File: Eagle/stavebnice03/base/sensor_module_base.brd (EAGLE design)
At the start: 19 parts

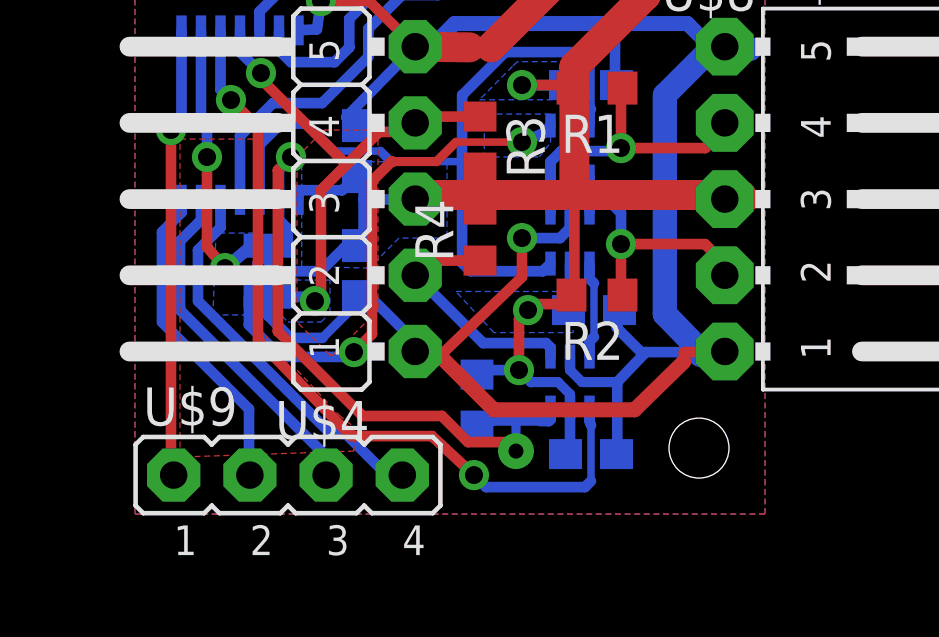
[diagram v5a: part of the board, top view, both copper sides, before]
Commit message: fix of bugs on rgb and lipol board + a few minor changes
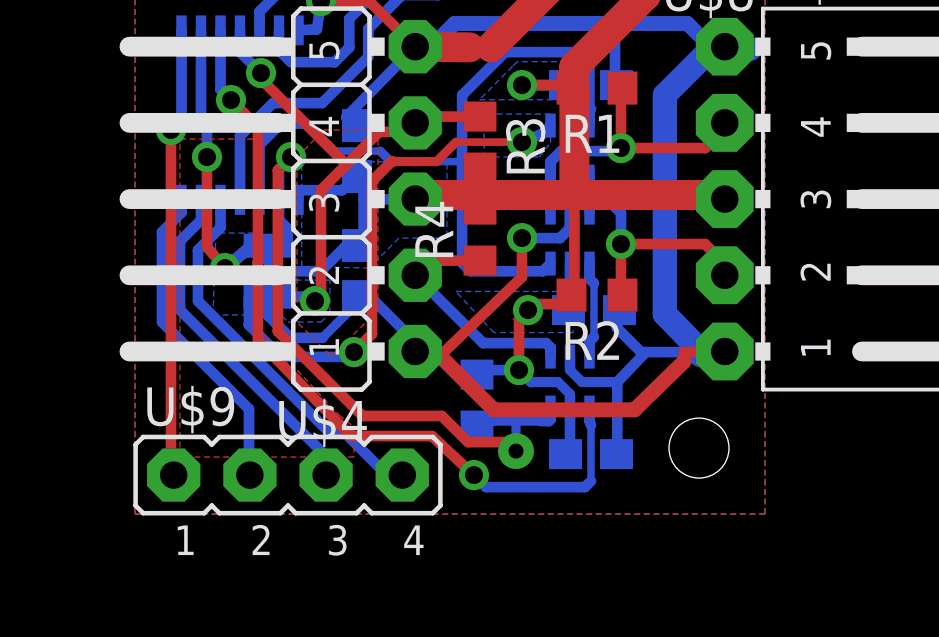
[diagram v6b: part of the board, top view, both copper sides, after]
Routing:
- net VCC: track 55.0 -> 53.9 mm
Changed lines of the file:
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@@
 <layer number="17" name="Pads" color="2" fill="1" visible="yes" active="yes"/>
 <layer number="18" name="Vias" color="2" fill="1" visible="yes" active="yes"/>
-<layer number="19" name="Unrouted" color="6" fill="1" visible="yes" active="yes"/>
+<layer number="19" name="Unrouted" color="6" fill="1" visible="no" active="yes"/>
 <layer number="20" name="Dimension" color="15" fill="1" visible="yes" active="yes"/>
 <layer number="21" name="tPlace" color="7" fill="1" visible="no" active="yes"/>
@@
 <text x="4.92125" y="-6.0325" size="2.54" layer="1" align="center">II=I+I</text>
 <text x="10.5" y="27" size="1.778" layer="20" align="center">sensor base</text>
-<wire x1="-10" y1="-10" x2="31" y2="-10" width="0.01" layer="49"/>
-<wire x1="31" y1="-10" x2="31" y2="31" width="0.01" layer="49"/>
-<wire x1="31" y1="31" x2="-10" y2="31" width="0.01" layer="49"/>
-<wire x1="-10" y1="31" x2="-10" y2="-10" width="0.01" layer="49"/>
+<wire x1="-10" y1="-10" x2="-2.5" y2="-10" width="0.01" layer="49"/>
+<wire x1="-2.5" y1="-10" x2="23.5" y2="-10" width="0.01" layer="49"/>
+<wire x1="23.5" y1="-10" x2="31" y2="-10" width="0.01" layer="49"/>
+<wire x1="31" y1="31" x2="23.5" y2="31" width="0.01" layer="49"/>
+<wire x1="23.5" y1="31" x2="-2.5" y2="31" width="0.01" layer="49"/>
+<wire x1="-2.5" y1="31" x2="-10" y2="31" width="0.01" layer="49"/>
 <circle x="2.2" y="18.8" radius="0.6" width="0.9" layer="116"/>
 <circle x="18.8" y="2.2" radius="0.6" width="0.9" layer="116"/>
@@
 <circle x="13.1" y="6.8" radius="0.25" width="0.2" layer="116"/>
 <circle x="12.8" y="4.8" radius="0.25" width="0.2" layer="116"/>
+<wire x1="-2.5" y1="31" x2="-2.5" y2="-10" width="0.01" layer="49"/>
+<wire x1="23.5" y1="31" x2="23.5" y2="-10" width="0.01" layer="49"/>
+<wire x1="-10" y1="-5" x2="-10" y2="-10" width="0.01" layer="49"/>
+<wire x1="-10" y1="26" x2="-10" y2="31" width="0.01" layer="49"/>
+<wire x1="31" y1="25.8" x2="31" y2="30.8" width="0.01" layer="49"/>
+<wire x1="31" y1="-5" x2="31" y2="-10" width="0.01" layer="49"/>
 </plain>
 <attributes>
@@
 <wire x1="14.64625" y1="10.63625" x2="14.805" y2="10.63625" width="0.8128" layer="1"/>
 <wire x1="14.805" y1="10.63625" x2="17.6625" y2="10.63625" width="1" layer="1"/>
-<wire x1="17.6625" y1="10.63625" x2="20.20875" y2="10.63625" width="1" layer="1"/>
-<wire x1="20.20875" y1="10.63625" x2="20.39125" y2="10.4775" width="0.8128" layer="1"/>
-<wire x1="20.39125" y1="10.4775" x2="19.66" y2="10.5" width="0.8128" layer="1"/>
+<wire x1="17.6625" y1="10.63625" x2="19.70875" y2="10.63625" width="1" layer="1"/>
+<wire x1="19.70875" y1="10.63625" x2="19.79125" y2="10.4775" width="0.8128" layer="1"/>
+<wire x1="19.79125" y1="10.4775" x2="19.66" y2="10.5" width="0.8128" layer="1"/>
 <via x="12.9" y="14.3" extent="1-16" drill="0.6"/>
 <wire x1="14.64625" y1="14.12875" x2="14.64625" y2="13.81125" width="0.3556" layer="1"/>
@@
 <vertex x="6.8" y="3.3"/>
 <vertex x="7.3" y="2.9"/>
-<vertex x="7.3" y="2.1"/>
+<vertex x="7.3" y="1.9"/>
 <vertex x="1.5" y="1.9"/>
 </polygon>

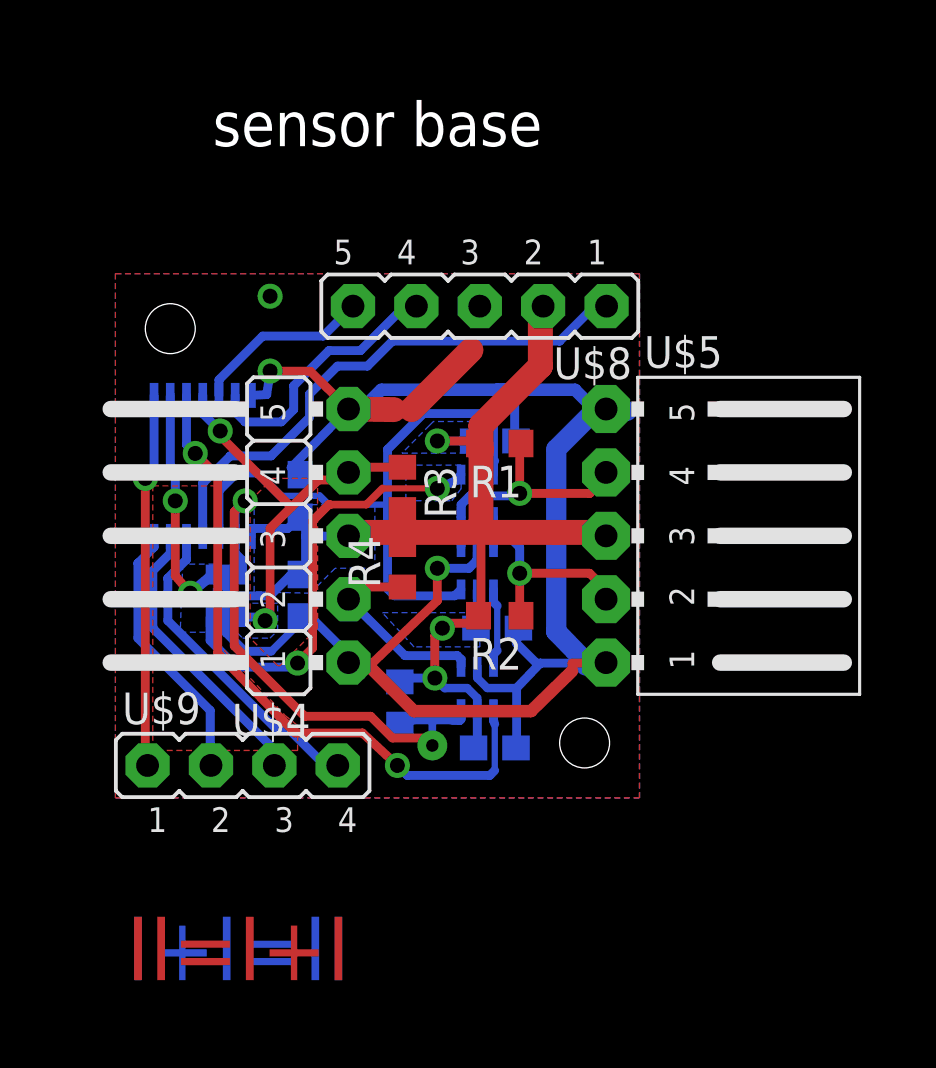
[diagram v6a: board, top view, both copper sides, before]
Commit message: C0603 changed to C0603K with wider space between soldering areas
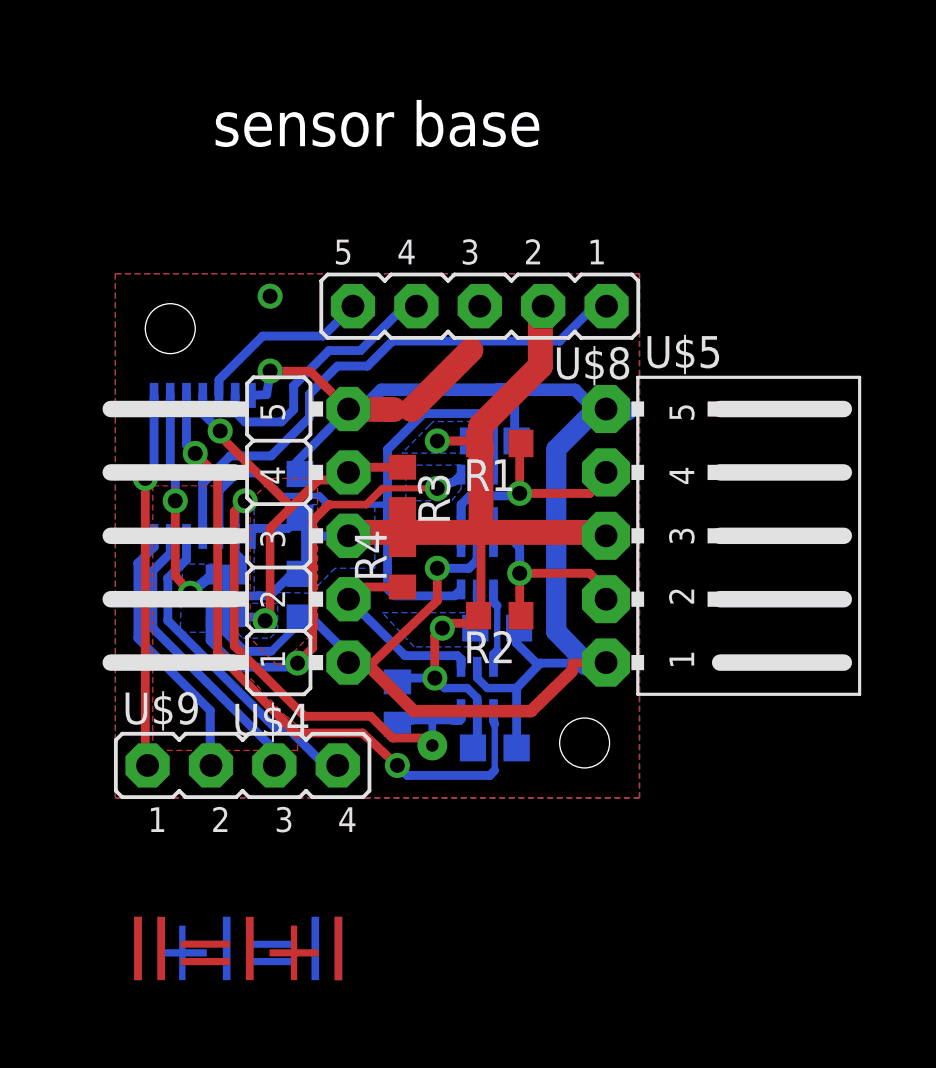
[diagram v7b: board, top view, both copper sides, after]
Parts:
- C1, C2, C3, C4, C5: device resistor:C0603 -> resistor:C0603K
- moved R5 0.10 mm to (11.3, 3.80)

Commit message: element position changed to be able put the bords to boxes + reset button for source board
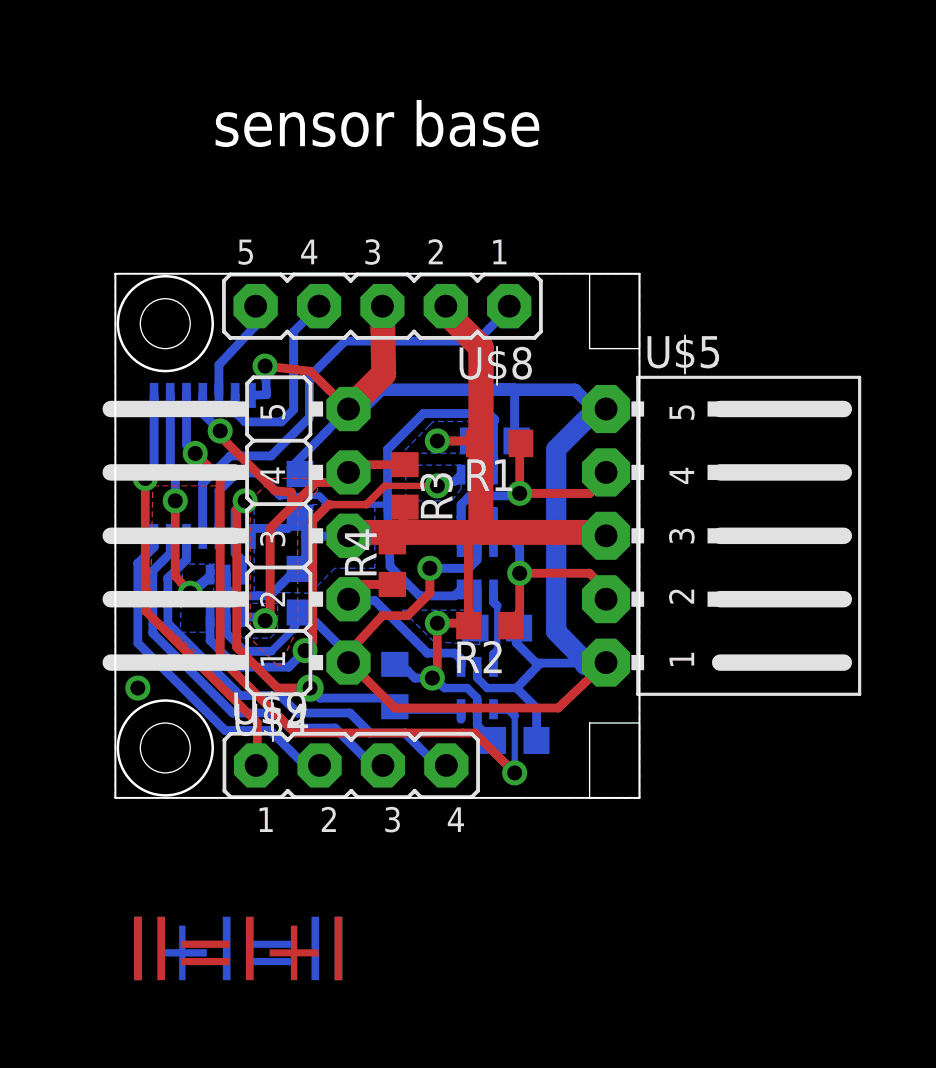
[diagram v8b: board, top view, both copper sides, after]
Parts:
- moved U$9 4.35 mm to (9.45, 1.30)
- moved U$8 3.90 mm to (10.7, 19.7)
- moved C4 0.85 mm to (16.0, 2.30)
- moved R5 0.71 mm to (11.2, 4.50)
- moved R2 0.57 mm to (15.0, 6.90)
- moved R4 0.41 mm to (11.1, 9.40)
- moved C1 0.20 mm to (7.40, 8.30)
- moved R3 0.14 mm to (11.6, 12.5)
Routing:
- net N$12: track 12.9 -> 17.3 mm
- net N$17: track 11.5 -> 15.6 mm
- net GND: track 82.8 -> 78.8 mm
- net N$13: track 21.8 -> 18.4 mm
- net N$9: track 23.0 -> 19.7 mm
- net N$3: track 10.9 -> 14.1 mm
- net N$15: track 7.22 -> 4.15 mm
- net N$14: track 10.6 -> 7.94 mm
- net N$18: track 15.0 -> 16.8 mm
- net N$4: track 26.5 -> 28.0 mm
- net N$10: track 10.1 -> 11.0 mm
- net N$1: track 25.4 -> 24.8 mm
- net N$11: track 16.9 -> 17.5 mm
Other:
- board outline added: 21 x 21 mm
- board text added: "ma-na-bu"
